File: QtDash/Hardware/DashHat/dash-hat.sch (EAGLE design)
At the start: 167 parts, among them IC1 LMV614, IC2 MCP3X083008, IC3 MCP23017SS, IC4 LM358D, IC5 IL300, IC6 TSV912D, IC7 IL300, IC8 TSV912D, IC9 DS1374, J1 CONN_20X2, J10 455-1750-1-ND, J15 VSS_IN, J16 TACH_IN, J6 VOLVO_CONN_31, J7 VOLVO_CONN_32, J8 455-1750-1-ND, Y1 ECX-.327-6-34RR

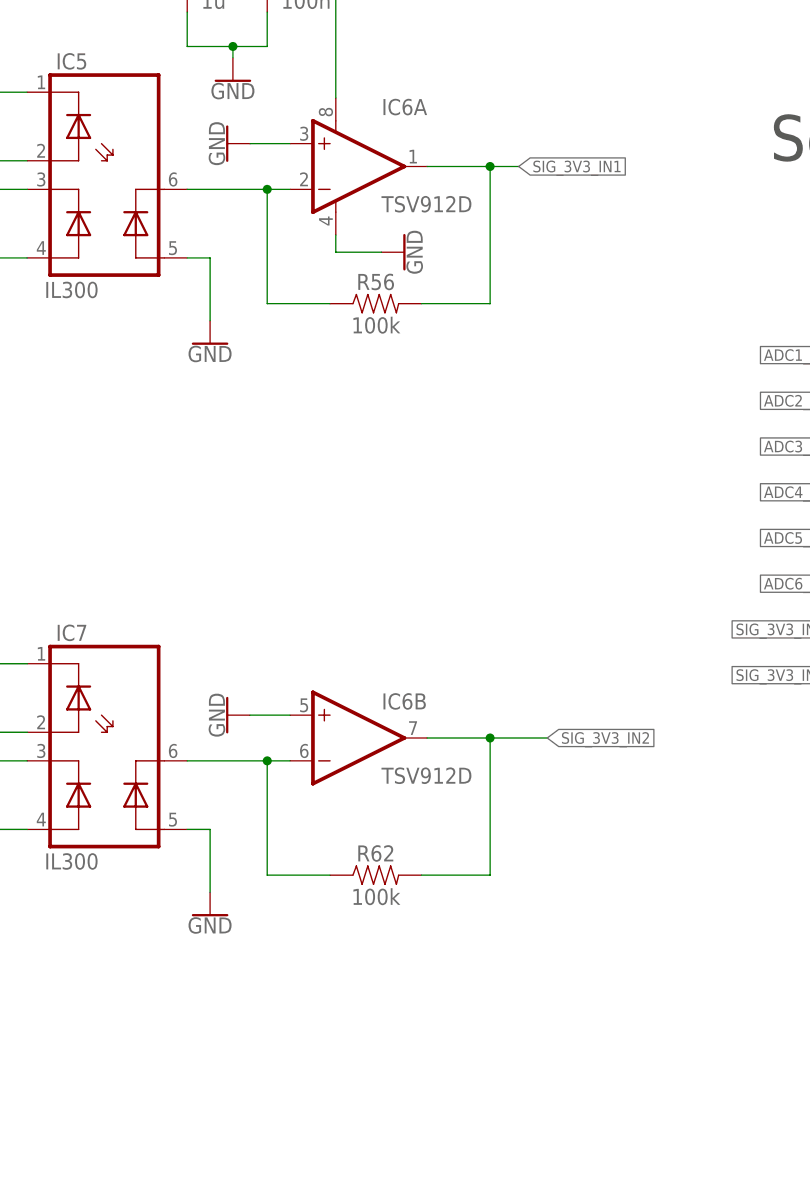
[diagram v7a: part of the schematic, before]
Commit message: bugfix/hardware-revA-issues: 	- output of IL300s were oscillating under load -- added 100n capacitor (bodged on revA) 	- 12V inputs are only 0-3.3V signals -- K3 used to compensate for different for now
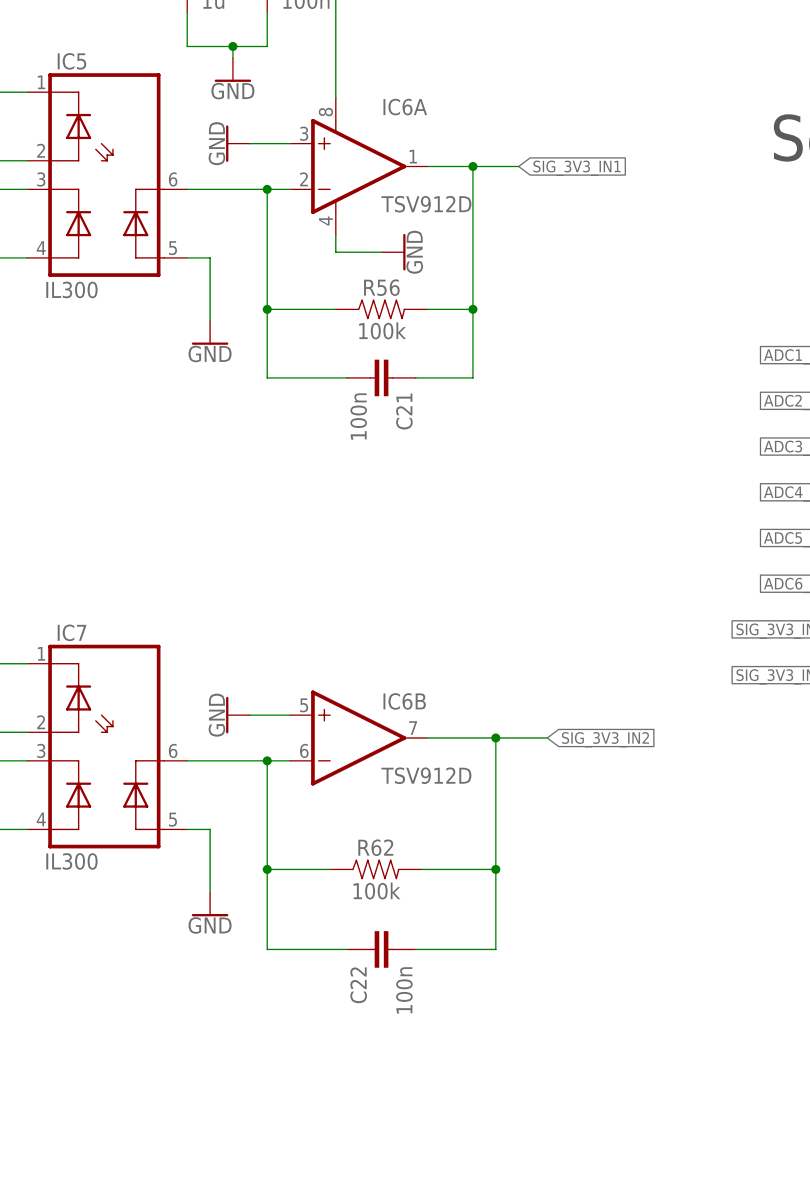
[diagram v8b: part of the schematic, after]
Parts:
- added C21, C22: 100n, digital_dash:CL10B104MB8NNNC
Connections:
- removed net N$18: IC5.C6, IC6A.-IN, R56.1
- new net N$10: C21.2, IC5.C6, IC6A.-IN, R56.1
- net N$27: now also C22.1
- net SIG_3V3_IN1: now also C21.1
- net SIG_3V3_IN2: now also C22.2
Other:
- moved on the sheet: R56, R62
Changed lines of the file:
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@@
 <part name="SUPPLY57" library="SparkFun-PowerSymbols" deviceset="12V" device=""/>
 <part name="J9" library="SparkFun-Connectors" deviceset="CONN_02" device="PTH4"/>
+<part name="C21" library="digital_dash" deviceset="CL" device="" technology="10B104MB8NNNC" value="100n"/>
+<part name="C22" library="digital_dash" deviceset="CL" device="" technology="10B104MB8NNNC" value="100n"/>
 </parts>
 <sheets>
@@
 <instance part="GND54" gate="1" x="285.75" y="255.27" rot="MR0"/>
 <instance part="GND55" gate="1" x="287.655" y="277.495" rot="MR90"/>
-<instance part="R56" gate="G$1" x="304.165" y="259.715"/>
+<instance part="R56" gate="G$1" x="304.8" y="259.08"/>
 <instance part="IC6" gate="B" x="302.26" y="211.455"/>
 <instance part="IC6" gate="A" x="302.26" y="274.955"/>
@@
 <instance part="GND61" gate="1" x="285.75" y="191.77" rot="MR0"/>
 <instance part="GND62" gate="1" x="287.655" y="213.995" rot="MR90"/>
-<instance part="R62" gate="G$1" x="304.165" y="196.215"/>
+<instance part="R62" gate="G$1" x="304.165" y="196.85"/>
 <instance part="IC4" gate="B" x="229.87" y="212.09"/>
 <instance part="IC4" gate="A" x="229.87" y="275.59"/>
@@
 <instance part="SUPPLY57" gate="G$1" x="454.66" y="289.56"/>
 <instance part="J9" gate="G$1" x="411.48" y="153.67"/>
+<instance part="C21" gate="G$1" x="303.53" y="251.46" rot="R270"/>
+<instance part="C22" gate="G$1" x="306.07" y="187.96" smashed="yes" rot="R90">
+<attribute name="NAME" x="303.149" y="181.864" size="1.778" layer="95" font="vector" rot="R90"/>
+<attribute name="VALUE" x="308.229" y="180.594" size="1.778" layer="96" font="vector" rot="R90"/>
+</instance>
 </instances>
 <busses>
@@
 <net name="SIG_3V3_IN1" class="0">
 <segment>
-<wire x1="309.245" y1="259.715" x2="316.865" y2="259.715" width="0.1524" layer="91"/>
-<wire x1="316.865" y1="259.715" x2="316.865" y2="274.955" width="0.1524" layer="91"/>
-<wire x1="316.865" y1="274.955" x2="309.88" y2="274.955" width="0.1524" layer="91"/>
+<wire x1="309.88" y1="259.08" x2="314.96" y2="259.08" width="0.1524" layer="91"/>
+<wire x1="314.96" y1="259.08" x2="314.96" y2="274.955" width="0.1524" layer="91"/>
+<wire x1="314.96" y1="274.955" x2="309.88" y2="274.955" width="0.1524" layer="91"/>
 <pinref part="R56" gate="G$1" pin="2"/>
-<wire x1="316.865" y1="274.955" x2="320.04" y2="274.955" width="0.1524" layer="91"/>
-<junction x="316.865" y="274.955"/>
+<wire x1="314.96" y1="274.955" x2="320.04" y2="274.955" width="0.1524" layer="91"/>
+<junction x="314.96" y="274.955"/>
 <label x="320.04" y="274.955" size="1.27" layer="95" xref="yes"/>
 <pinref part="IC6" gate="A" pin="OUT"/>
+<pinref part="C21" gate="G$1" pin="1"/>
+<wire x1="308.61" y1="251.46" x2="314.96" y2="251.46" width="0.1524" layer="91"/>
+<wire x1="314.96" y1="251.46" x2="314.96" y2="259.08" width="0.1524" layer="91"/>
+<junction x="314.96" y="259.08"/>
 </segment>
 <segment>
@@
 <pinref part="IC2" gate="G$1" pin="CH6"/>
 <wire x1="355.6" y1="223.52" x2="364.49" y2="223.52" width="0.1524" layer="91"/>
-</segment>
-</net>
-<net name="N$18" class="0">
-<segment>
-<pinref part="R56" gate="G$1" pin="1"/>
-<pinref part="IC5" gate="G$1" pin="C6"/>
-<wire x1="283.21" y1="272.415" x2="292.1" y2="272.415" width="0.1524" layer="91"/>
-<wire x1="292.1" y1="272.415" x2="294.64" y2="272.415" width="0.1524" layer="91"/>
-<junction x="292.1" y="272.415"/>
-<wire x1="292.1" y1="272.415" x2="292.1" y2="259.715" width="0.1524" layer="91"/>
-<wire x1="292.1" y1="259.715" x2="299.085" y2="259.715" width="0.1524" layer="91"/>
-<pinref part="IC6" gate="A" pin="-IN"/>
 </segment>
 </net>
@@
 <net name="SIG_3V3_IN2" class="0">
 <segment>
-<wire x1="309.245" y1="196.215" x2="316.865" y2="196.215" width="0.1524" layer="91"/>
-<wire x1="316.865" y1="196.215" x2="316.865" y2="211.455" width="0.1524" layer="91"/>
+<wire x1="309.245" y1="196.85" x2="317.5" y2="196.85" width="0.1524" layer="91"/>
+<wire x1="317.5" y1="196.85" x2="317.5" y2="211.455" width="0.1524" layer="91"/>
 <pinref part="R62" gate="G$1" pin="2"/>
 <pinref part="IC6" gate="B" pin="OUT"/>
-<wire x1="309.88" y1="211.455" x2="316.865" y2="211.455" width="0.1524" layer="91"/>
-<wire x1="316.865" y1="211.455" x2="323.215" y2="211.455" width="0.1524" layer="91"/>
-<junction x="316.865" y="211.455"/>
+<wire x1="309.88" y1="211.455" x2="317.5" y2="211.455" width="0.1524" layer="91"/>
+<wire x1="317.5" y1="211.455" x2="323.215" y2="211.455" width="0.1524" layer="91"/>
+<junction x="317.5" y="211.455"/>
 <label x="323.215" y="211.455" size="1.27" layer="95" xref="yes"/>
+<pinref part="C22" gate="G$1" pin="2"/>
+<wire x1="308.61" y1="187.96" x2="317.5" y2="187.96" width="0.1524" layer="91"/>
+<wire x1="317.5" y1="187.96" x2="317.5" y2="196.85" width="0.1524" layer="91"/>
+<junction x="317.5" y="196.85"/>
 </segment>
 <segment>
@@
 <wire x1="292.1" y1="208.915" x2="294.64" y2="208.915" width="0.1524" layer="91"/>
 <junction x="292.1" y="208.915"/>
-<wire x1="292.1" y1="208.915" x2="292.1" y2="196.215" width="0.1524" layer="91"/>
-<wire x1="292.1" y1="196.215" x2="299.085" y2="196.215" width="0.1524" layer="91"/>
+<wire x1="292.1" y1="208.915" x2="292.1" y2="196.85" width="0.1524" layer="91"/>
+<wire x1="292.1" y1="196.85" x2="299.085" y2="196.85" width="0.1524" layer="91"/>
 <pinref part="IC6" gate="B" pin="-IN"/>
+<pinref part="C22" gate="G$1" pin="1"/>
+<wire x1="300.99" y1="187.96" x2="292.1" y2="187.96" width="0.1524" layer="91"/>
+<wire x1="292.1" y1="187.96" x2="292.1" y2="196.85" width="0.1524" layer="91"/>
+<junction x="292.1" y="196.85"/>
 </segment>
 </net>
@@
 </segment>
 </net>
+<net name="N$10" class="0">
+<segment>
+<pinref part="C21" gate="G$1" pin="2"/>
+<wire x1="300.99" y1="251.46" x2="292.1" y2="251.46" width="0.1524" layer="91"/>
+<pinref part="R56" gate="G$1" pin="1"/>
+<pinref part="IC5" gate="G$1" pin="C6"/>
+<wire x1="283.21" y1="272.415" x2="292.1" y2="272.415" width="0.1524" layer="91"/>
+<wire x1="292.1" y1="272.415" x2="294.64" y2="272.415" width="0.1524" layer="91"/>
+<junction x="292.1" y="272.415"/>
+<wire x1="292.1" y1="272.415" x2="292.1" y2="259.08" width="0.1524" layer="91"/>
+<wire x1="292.1" y1="259.08" x2="299.72" y2="259.08" width="0.1524" layer="91"/>
+<pinref part="IC6" gate="A" pin="-IN"/>
+<wire x1="292.1" y1="251.46" x2="292.1" y2="259.08" width="0.1524" layer="91"/>
+<junction x="292.1" y="259.08"/>
+</segment>
+</net>
